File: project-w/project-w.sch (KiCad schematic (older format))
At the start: 17 parts, among them U1 NE555, U2 CD4017

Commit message: adding trace routes
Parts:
- removed BT1: Battery_Cell, Connectors_USB:USB_Micro-B_Wuerth-629105150521, symbol Battery_Cell
- added J1: USB_A, Connectors_USB:USB_Micro-B_Molex-105017-0001, symbol USB_A
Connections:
- net at R2.1, U1.4 (R), U1.8 (VCC): now also J1.1 (VBUS)
- net at C1.2, R3.2, U1.1 (GND)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: now also J1.4 (GND)
- no-connect marks 2 -> 5
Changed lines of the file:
@@
 Connection ~ 4200 3050
 Connection ~ 4200 2900
+Wire Wire Line
+	4600 4150 4600 4950
 $Comp
-L Battery_Cell BT1
-U 1 1 5A66093F
-P 2150 3600
-F 0 "BT1" H 2250 3700 50  0000 L CNN
-F 1 "Battery_Cell" H 2250 3600 50  0000 L CNN
-F 2 "Connectors_USB:USB_Micro-B_Wuerth-629105150521" V 2150 3660 50  0001 C CNN
-F 3 "" V 2150 3660 50  0001 C CNN
-	1    2150 3600
+L USB_A J1
+U 1 1 5A67207D
+P 2150 2950
+F 0 "J1" H 1950 3400 50  0000 L CNN
+F 1 "USB_A" H 1950 3300 50  0000 L CNN
+F 2 "Connectors_USB:USB_Micro-B_Molex-105017-0001" H 2300 2900 50  0001 C CNN
+F 3 "" H 2300 2900 50  0001 C CNN
+	1    2150 2950
 	1    0    0    -1
 $EndComp
 Wire Wire Line
-	4200 2750 2150 2750
+	2150 3350 2150 4950
 Wire Wire Line
-	2150 2750 2150 3400
-Wire Wire Line
-	4600 4150 4600 4950
-Wire Wire Line
-	2150 4950 2150 3700
+	2450 2750 4200 2750
+NoConn ~ 2450 2950
+NoConn ~ 2450 3050
+NoConn ~ 2050 3350
 $EndSCHEMATC

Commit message: adding more space for silk screening
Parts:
- U1: footprint Housings_DIP:DIP-8_W7.62mm_Socket -> Housings_DIP:DIP-8_W7.62mm
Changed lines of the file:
@@
 F 0 "U1" H 3800 4100 50  0000 L CNN
 F 1 "NE555" H 4300 4100 50  0000 L CNN
-F 2 "Housings_DIP:DIP-8_W7.62mm_Socket" H 4200 3750 50  0001 C CNN
+F 2 "Housings_DIP:DIP-8_W7.62mm" H 4200 3750 50  0001 C CNN
 F 3 "" H 4200 3750 50  0001 C CNN
 	1    4200 3750

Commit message: trying to fix 3d models
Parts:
- J1: footprint Connectors_USB:USB_Micro-B_Molex-105017-0001 -> Connectors_USB:USB_Micro-B_Molex_47346-0001
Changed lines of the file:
@@
 F 0 "J1" H 1950 3400 50  0000 L CNN
 F 1 "USB_A" H 1950 3300 50  0000 L CNN
-F 2 "Connectors_USB:USB_Micro-B_Molex-105017-0001" H 2300 2900 50  0001 C CNN
+F 2 "Connectors_USB:USB_Micro-B_Molex_47346-0001" H 2300 2900 50  0001 C CNN
 F 3 "" H 2300 2900 50  0001 C CNN
 	1    2150 2950

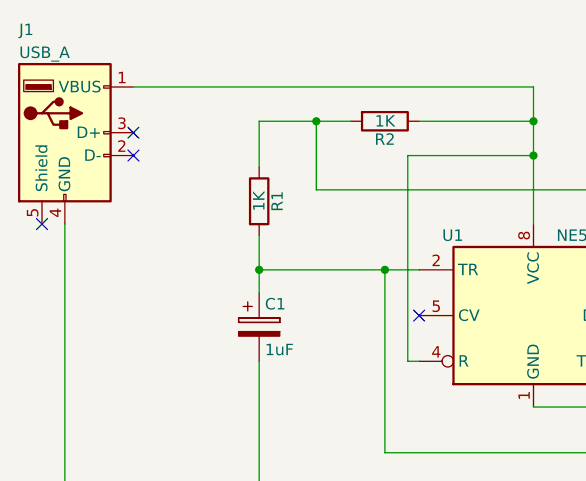
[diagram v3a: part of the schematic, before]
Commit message: updating schematic to fix VSS VDD issues
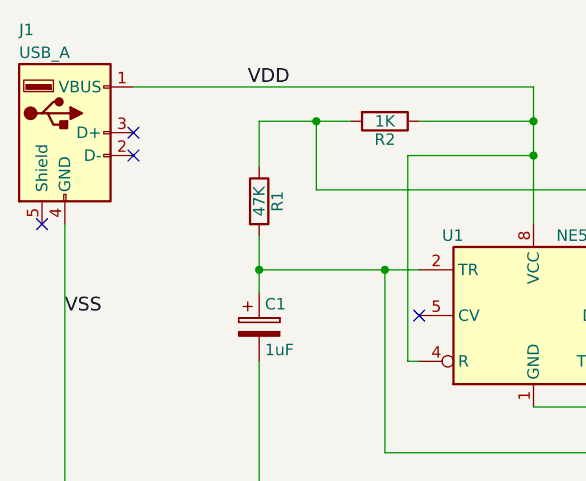
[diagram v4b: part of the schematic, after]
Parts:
- R1: value 1K -> 47K
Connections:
- net VDD: now also J1.1 (VBUS), R2.1, U1.4 (R), U1.8 (VCC)
- net VSS: now also C1.2, J1.4 (GND), R3.2, U1.1 (GND), U2.13 (CKEN), U2.15 (Reset)
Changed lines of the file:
@@
 P 3000 3250
 F 0 "R1" V 3080 3250 50  0000 C CNN
-F 1 "1K" V 3000 3250 50  0000 C CNN
+F 1 "47K" V 3000 3250 50  0000 C CNN
 F 2 "Resistors_THT:R_Axial_DIN0207_L6.3mm_D2.5mm_P7.62mm_Horizontal" V 2930 3250 50  0001 C CNN
 F 3 "" H 3000 3250 50  0001 C CNN
@@
 NoConn ~ 2450 3050
 NoConn ~ 2050 3350
+Text Label 2950 2750 0    60   ~ 0
+VDD
+Text Label 2150 3750 0    60   ~ 0
+VSS
 $EndSCHEMATC

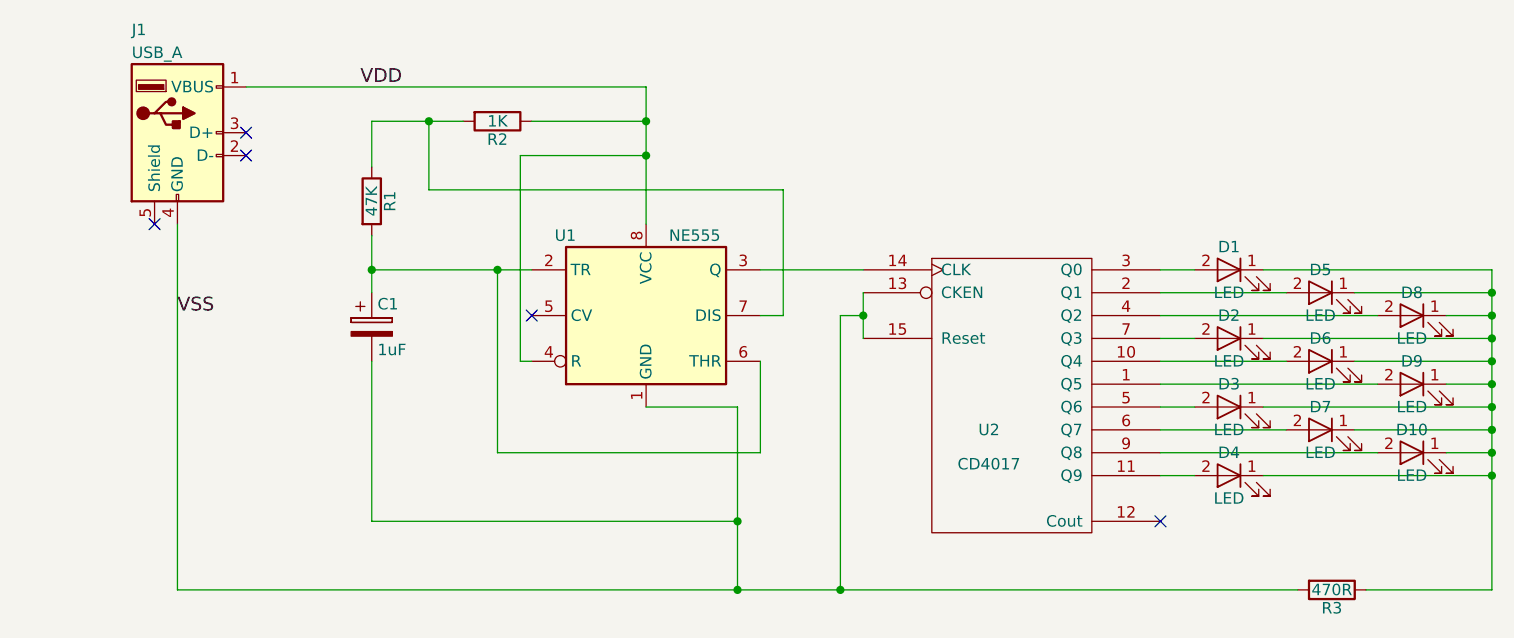
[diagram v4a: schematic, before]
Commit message: updating schematic, fixing ordering issues, changin power connection
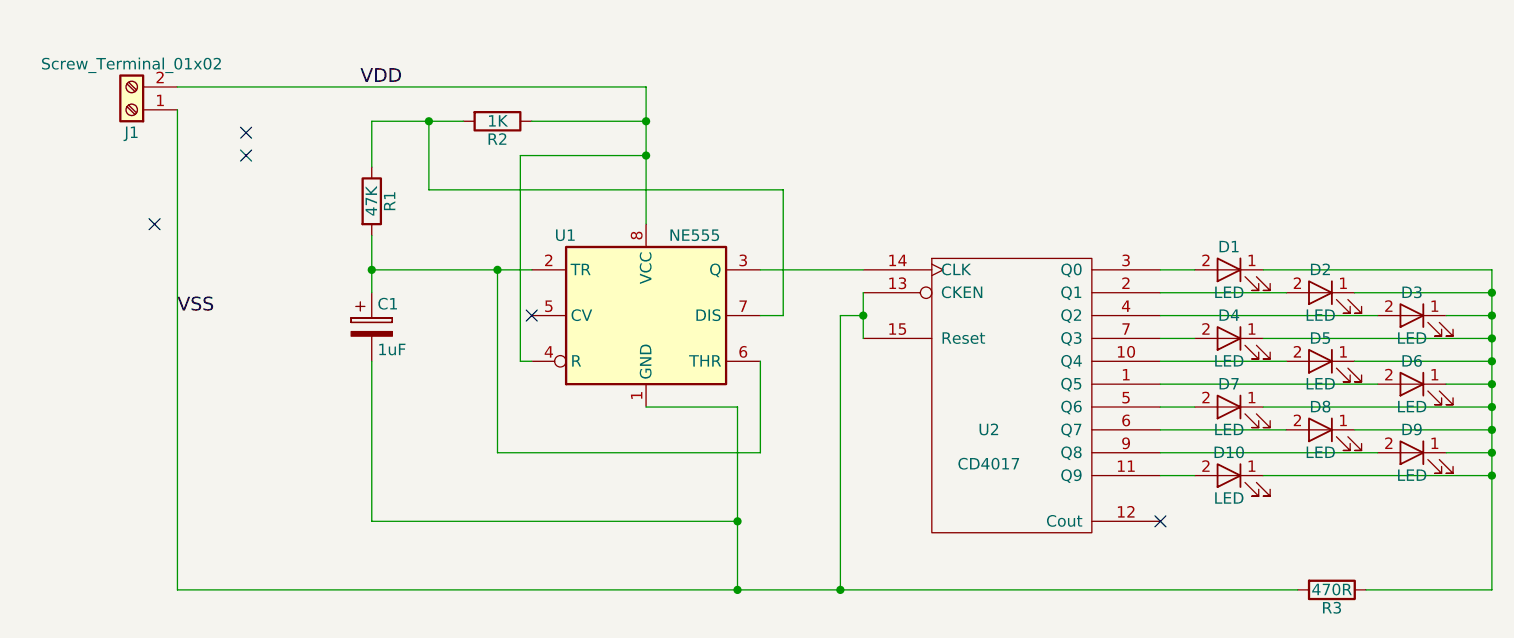
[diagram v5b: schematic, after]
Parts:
- removed J1: USB_A, Connectors_USB:USB_Micro-B_Molex_47346-0001, symbol USB_A
- added J1: Screw_Terminal_01x02, Connectors_Terminal_Blocks:TerminalBlock_bornier-2_P5.08mm, symbol Screw_Terminal_01x02
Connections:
- net VDD: now also J1.2 (Pin_2)
- net VSS: now also J1.1 (Pin_1)
- net at U2.1 (Q5): now also D6.2 (A); no longer D9.2 (A)
- net at U2.10 (Q4): now also D5.2 (A); no longer D6.2 (A)
- net at U2.11 (Q9): now also D10.2 (A); no longer D4.2 (A)
- net at U2.2 (Q1): now also D2.2 (A); no longer D5.2 (A)
- net at U2.4 (Q2): now also D3.2 (A); no longer D8.2 (A)
- net at U2.5 (Q6): now also D7.2 (A); no longer D3.2 (A)
- net at U2.6 (Q7): now also D8.2 (A); no longer D7.2 (A)
- net at U2.7 (Q3): now also D4.2 (A); no longer D2.2 (A)
- net at U2.9 (Q8): now also D9.2 (A); no longer D10.2 (A)
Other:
- moved on the sheet: D10, D2, D3, D4, D5, D6, D7, D8, D9
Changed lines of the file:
@@
 L LED D5
 U 1 1 5A65E7B7
+P 7150 3950
+F 0 "D5" H 7150 4050 50  0000 C CNN
+F 1 "LED" H 7150 3850 50  0000 C CNN
+F 2 "LEDs:LED_D3.0mm" H 7150 3950 50  0001 C CNN
+F 3 "" H 7150 3950 50  0001 C CNN
+	1    7150 3950
+	-1   0    0    -1
+$EndComp
+$Comp
+L LED D8
+U 1 1 5A65E881
+P 7150 4250
+F 0 "D8" H 7150 4350 50  0000 C CNN
+F 1 "LED" H 7150 4150 50  0000 C CNN
+F 2 "LEDs:LED_D3.0mm" H 7150 4250 50  0001 C CNN
+F 3 "" H 7150 4250 50  0001 C CNN
+	1    7150 4250
+	-1   0    0    -1
+$EndComp
+$Comp
+L LED D2
+U 1 1 5A65E8C6
 P 7150 3650
-F 0 "D5" H 7150 3750 50  0000 C CNN
+F 0 "D2" H 7150 3750 50  0000 C CNN
 F 1 "LED" H 7150 3550 50  0000 C CNN
 F 2 "LEDs:LED_D3.0mm" H 7150 3650 50  0001 C CNN
@@
 $EndComp
 $Comp
-L LED D8
-U 1 1 5A65E881
+L LED D6
+U 1 1 5A65E914
+P 7550 4050
+F 0 "D6" H 7550 4150 50  0000 C CNN
+F 1 "LED" H 7550 3950 50  0000 C CNN
+F 2 "LEDs:LED_D3.0mm" H 7550 4050 50  0001 C CNN
+F 3 "" H 7550 4050 50  0001 C CNN
+	1    7550 4050
+	-1   0    0    -1
+$EndComp
+$Comp
+L LED D9
+U 1 1 5A65E959
+P 7550 4350
+F 0 "D9" H 7550 4450 50  0000 C CNN
+F 1 "LED" H 7550 4250 50  0000 C CNN
+F 2 "LEDs:LED_D3.0mm" H 7550 4350 50  0001 C CNN
+F 3 "" H 7550 4350 50  0001 C CNN
+	1    7550 4350
+	-1   0    0    -1
+$EndComp
+$Comp
+L LED D3
+U 1 1 5A65E9A5
 P 7550 3750
-F 0 "D8" H 7550 3850 50  0000 C CNN
+F 0 "D3" H 7550 3850 50  0000 C CNN
 F 1 "LED" H 7550 3650 50  0000 C CNN
 F 2 "LEDs:LED_D3.0mm" H 7550 3750 50  0001 C CNN
@@
 $EndComp
 $Comp
-L LED D2
-U 1 1 5A65E8C6
+L LED D7
+U 1 1 5A65E9F4
+P 6750 4150
+F 0 "D7" H 6750 4250 50  0000 C CNN
+F 1 "LED" H 6750 4050 50  0000 C CNN
+F 2 "LEDs:LED_D3.0mm" H 6750 4150 50  0001 C CNN
+F 3 "" H 6750 4150 50  0001 C CNN
+	1    6750 4150
+	-1   0    0    -1
+$EndComp
+$Comp
+L LED D10
+U 1 1 5A65EA3C
+P 6750 4450
+F 0 "D10" H 6750 4550 50  0000 C CNN
+F 1 "LED" H 6750 4350 50  0000 C CNN
+F 2 "LEDs:LED_D3.0mm" H 6750 4450 50  0001 C CNN
+F 3 "" H 6750 4450 50  0001 C CNN
+	1    6750 4450
+	-1   0    0    -1
+$EndComp
+$Comp
+L LED D4
+U 1 1 5A65EA8D
 P 6750 3850
-F 0 "D2" H 6750 3950 50  0000 C CNN
+F 0 "D4" H 6750 3950 50  0000 C CNN
 F 1 "LED" H 6750 3750 50  0000 C CNN
 F 2 "LEDs:LED_D3.0mm" H 6750 3850 50  0001 C CNN
@@
 	-1   0    0    -1
 $EndComp
-$Comp
-L LED D6
-U 1 1 5A65E914
-P 7150 3950
-F 0 "D6" H 7150 4050 50  0000 C CNN
-F 1 "LED" H 7150 3850 50  0000 C CNN
-F 2 "LEDs:LED_D3.0mm" H 7150 3950 50  0001 C CNN
-F 3 "" H 7150 3950 50  0001 C CNN
-	1    7150 3950
-	-1   0    0    -1
-$EndComp
-$Comp
-L LED D9
-U 1 1 5A65E959
-P 7550 4050
-F 0 "D9" H 7550 4150 50  0000 C CNN
-F 1 "LED" H 7550 3950 50  0000 C CNN
-F 2 "LEDs:LED_D3.0mm" H 7550 4050 50  0001 C CNN
-F 3 "" H 7550 4050 50  0001 C CNN
-	1    7550 4050
-	-1   0    0    -1
-$EndComp
-$Comp
-L LED D3
-U 1 1 5A65E9A5
-P 6750 4150
-F 0 "D3" H 6750 4250 50  0000 C CNN
-F 1 "LED" H 6750 4050 50  0000 C CNN
-F 2 "LEDs:LED_D3.0mm" H 6750 4150 50  0001 C CNN
-F 3 "" H 6750 4150 50  0001 C CNN
-	1    6750 4150
-	-1   0    0    -1
-$EndComp
-$Comp
-L LED D7
-U 1 1 5A65E9F4
-P 7150 4250
-F 0 "D7" H 7150 4350 50  0000 C CNN
-F 1 "LED" H 7150 4150 50  0000 C CNN
-F 2 "LEDs:LED_D3.0mm" H 7150 4250 50  0001 C CNN
-F 3 "" H 7150 4250 50  0001 C CNN
-	1    7150 4250
-	-1   0    0    -1
-$EndComp
-$Comp
-L LED D10
-U 1 1 5A65EA3C
-P 7550 4350
-F 0 "D10" H 7550 4450 50  0000 C CNN
-F 1 "LED" H 7550 4250 50  0000 C CNN
-F 2 "LEDs:LED_D3.0mm" H 7550 4350 50  0001 C CNN
-F 3 "" H 7550 4350 50  0001 C CNN
-	1    7550 4350
-	-1   0    0    -1
-$EndComp
-$Comp
-L LED D4
-U 1 1 5A65EA8D
-P 6750 4450
-F 0 "D4" H 6750 4550 50  0000 C CNN
-F 1 "LED" H 6750 4350 50  0000 C CNN
-F 2 "LEDs:LED_D3.0mm" H 6750 4450 50  0001 C CNN
-F 3 "" H 6750 4450 50  0001 C CNN
-	1    6750 4450
-	-1   0    0    -1
-$EndComp
 NoConn ~ 6450 4650
 NoConn ~ 3700 3750
@@
 Wire Wire Line
 	4600 4150 4600 4950
-$Comp
-L USB_A J1
-U 1 1 5A67207D
-P 2150 2950
-F 0 "J1" H 1950 3400 50  0000 L CNN
-F 1 "USB_A" H 1950 3300 50  0000 L CNN
-F 2 "Connectors_USB:USB_Micro-B_Molex_47346-0001" H 2300 2900 50  0001 C CNN
-F 3 "" H 2300 2900 50  0001 C CNN
-	1    2150 2950
-	1    0    0    -1
-$EndComp
-Wire Wire Line
-	2150 3350 2150 4950
-Wire Wire Line
-	2450 2750 4200 2750
+Wire Wire Line
+	2150 2850 2150 4950
+Wire Wire Line
+	2150 2750 4200 2750
 NoConn ~ 2450 2950
 NoConn ~ 2450 3050
@@
 Text Label 2150 3750 0    60   ~ 0
 VSS
+$Comp
+L Screw_Terminal_01x02 J1
+U 1 1 5AFC9767
+P 1950 2850
+F 0 "J1" H 1950 2950 50  0000 C CNN
+F 1 "Screw_Terminal_01x02" H 1950 2650 50  0000 C CNN
+F 2 "Connectors_Terminal_Blocks:TerminalBlock_bornier-2_P5.08mm" H 1950 2850 50  0001 C CNN
+F 3 "" H 1950 2850 50  0001 C CNN
+	1    1950 2850
+	-1   0    0    1
+$EndComp
 $EndSCHEMATC

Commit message: fixes for prototype version 3
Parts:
- R3: value 470R -> 1K
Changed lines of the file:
@@
 P 7200 4950
 F 0 "R3" V 7280 4950 50  0000 C CNN
-F 1 "470R" V 7200 4950 50  0000 C CNN
+F 1 "1K" V 7200 4950 50  0000 C CNN
 F 2 "Resistors_THT:R_Axial_DIN0204_L3.6mm_D1.6mm_P5.08mm_Horizontal" V 7130 4950 50  0001 C CNN
 F 3 "" H 7200 4950 50  0001 C CNN
